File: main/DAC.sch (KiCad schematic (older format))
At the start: 14 parts, among them IC3 PCM1741E, J7 Breakout I2S

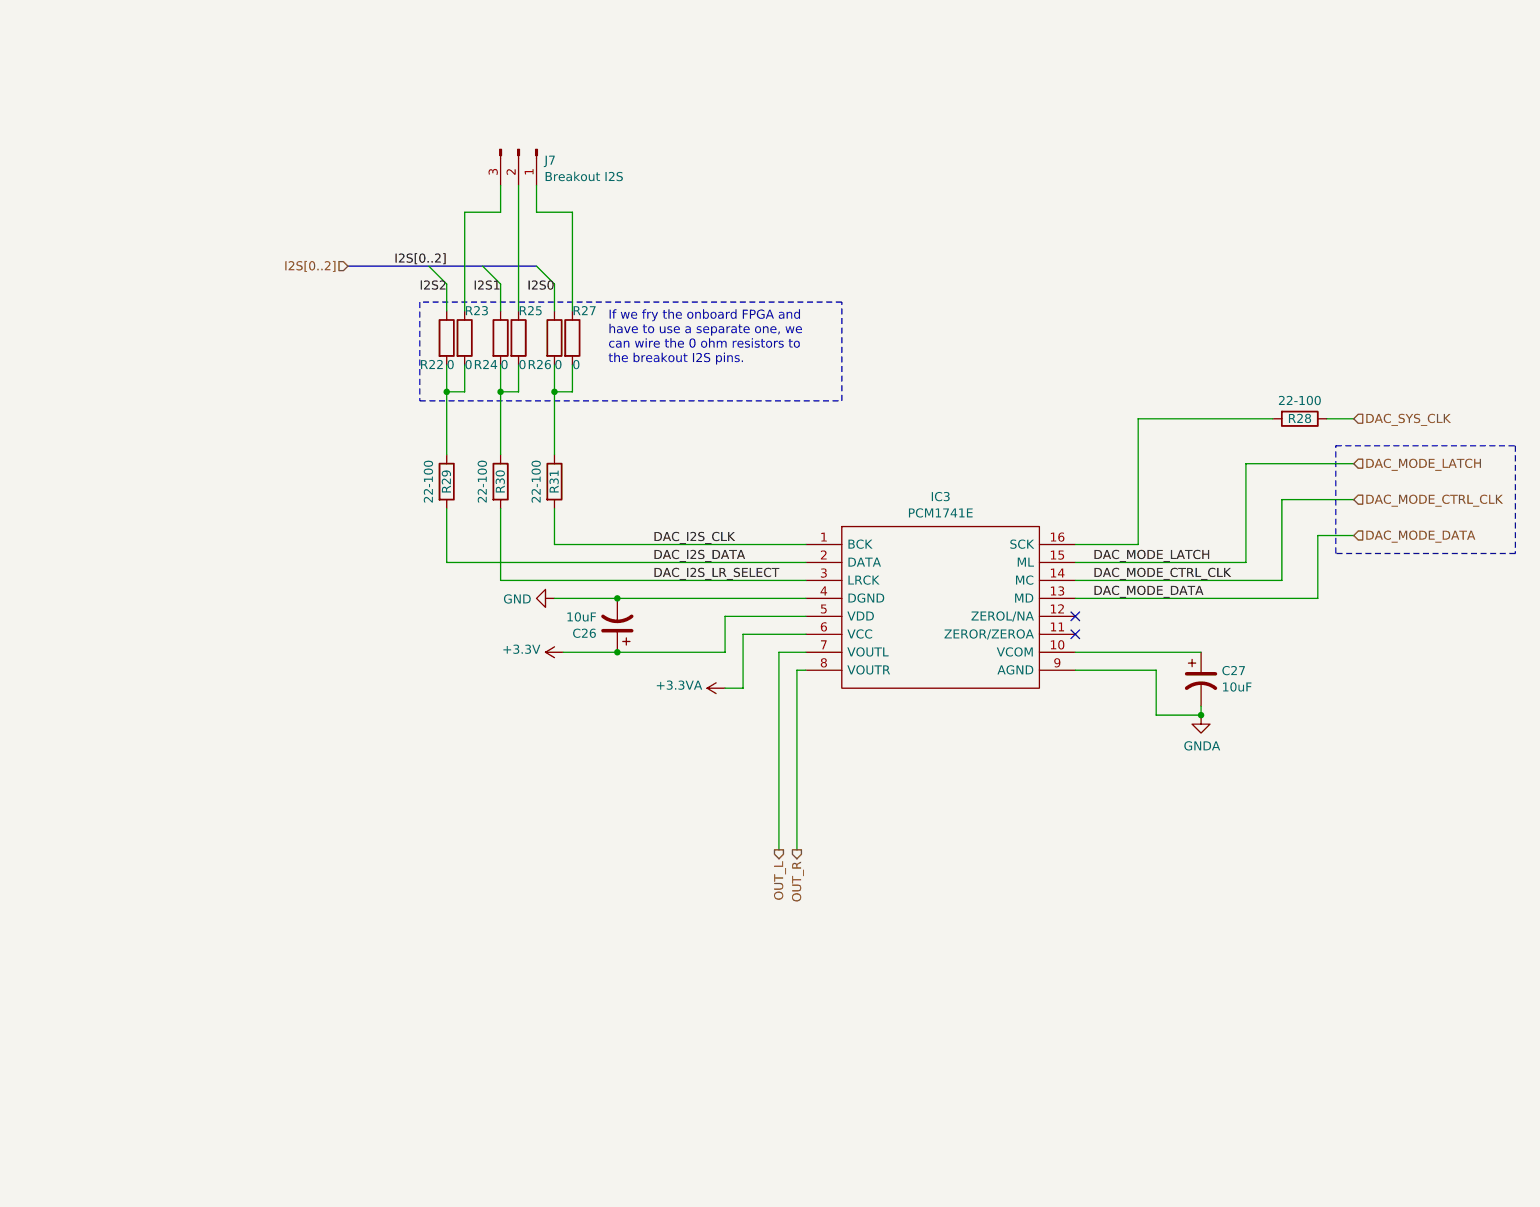
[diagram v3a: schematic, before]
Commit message: DAC: Remove amplifier, replace with low pass as per datasheet
Also: a lot of footprint association
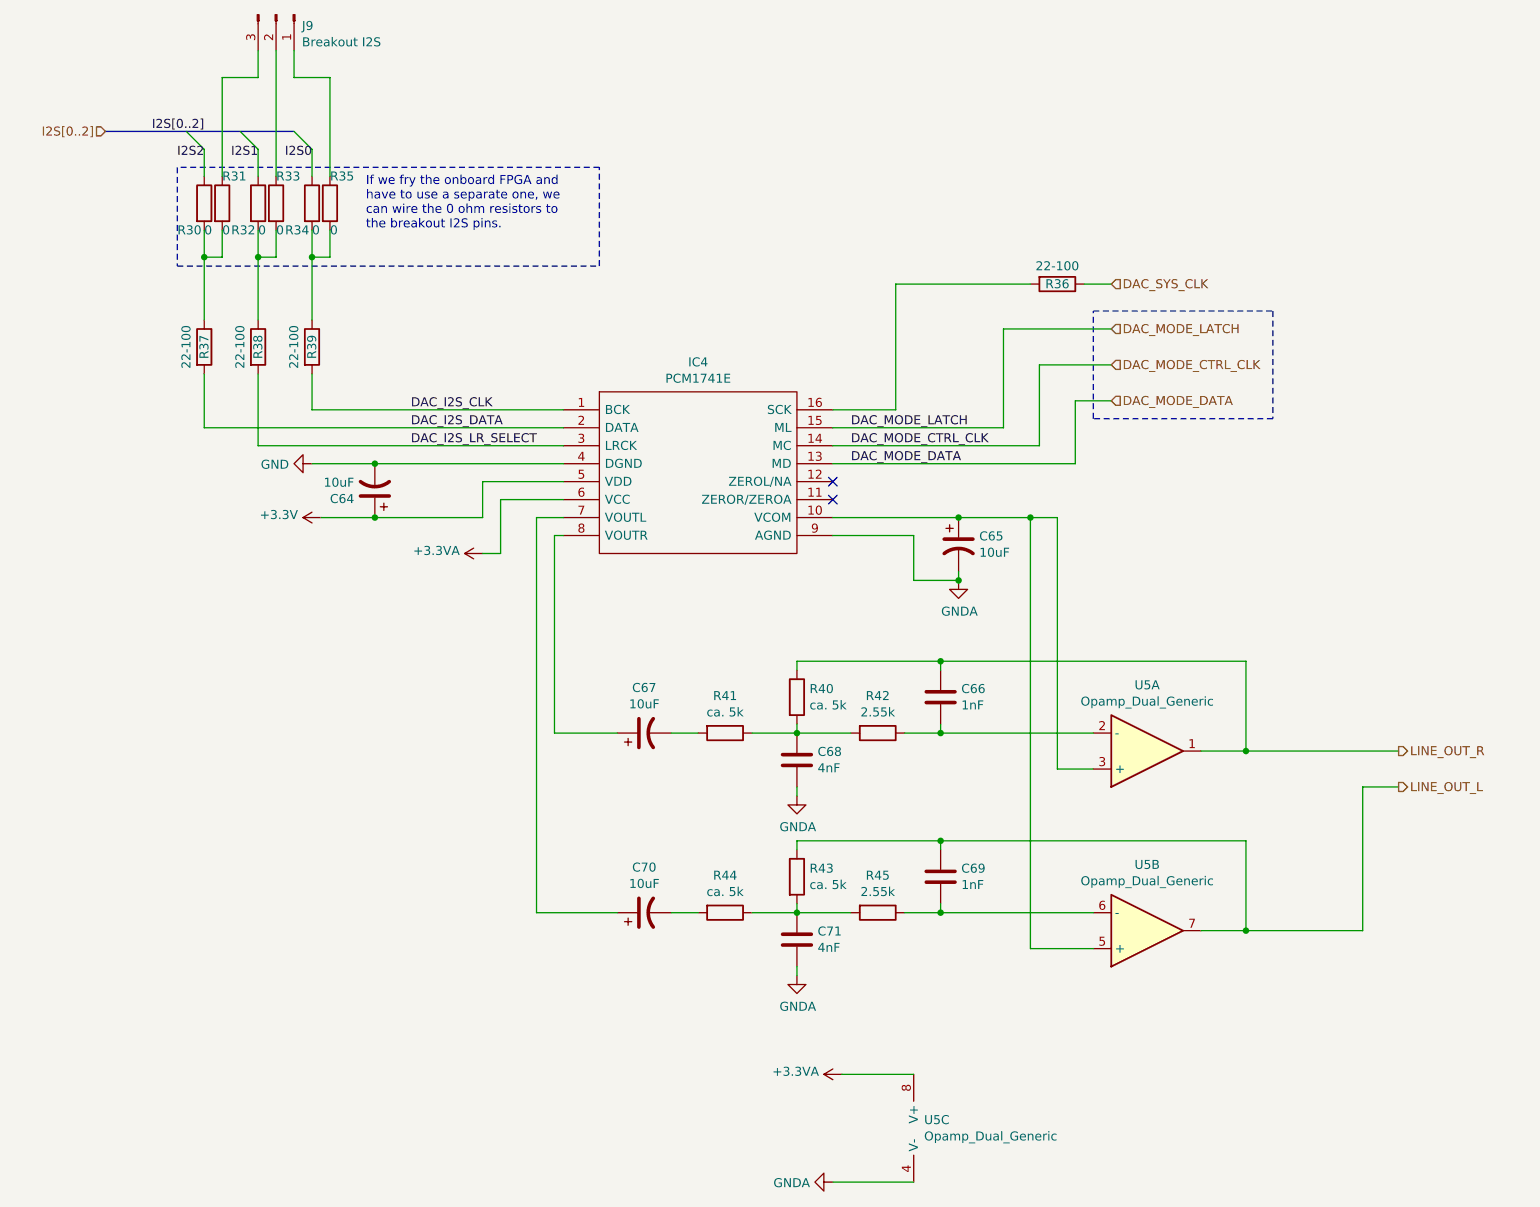
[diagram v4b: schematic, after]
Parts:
- added C66, C69: 1nF, Capacitor_SMD:C_0805_2012Metric_Pad1.18x1.45mm_HandSolder, symbol Device:C
- added C67, C70: 10uF, Capacitor_Tantalum_SMD:CP_EIA-3528-12_Kemet-T_Pad1.50x2.35mm_HandSolder, symbol Device:CP1
- added C68, C71: 4nF, Capacitor_SMD:C_0805_2012Metric_Pad1.18x1.45mm_HandSolder, symbol Device:C
- added R40, R41, R43, R44: ca. 5k, Resistor_SMD:R_0805_2012Metric_Pad1.20x1.40mm_HandSolder, symbol Device:R
- added R42, R45: 2.55k, Resistor_SMD:R_0805_2012Metric_Pad1.20x1.40mm_HandSolder, symbol Device:R
- added U5: Opamp_Dual_Generic, Package_SO:SOIC-8_5.23x5.23mm_P1.27mm, symbol Device:Opamp_Dual_Generic
- C64: renamed from C26; footprint (none) -> Capacitor_Tantalum_SMD:CP_EIA-3528-12_Kemet-T_Pad1.50x2.35mm_HandSolder
- C65: renamed from C27; footprint (none) -> Capacitor_Tantalum_SMD:CP_EIA-3528-12_Kemet-T_Pad1.50x2.35mm_HandSolder
- J9: renamed from J7; footprint (none) -> Connector_PinHeader_2.54mm:PinHeader_1x03_P2.54mm_Vertical
- renumbered IC3 to IC4, R22 to R30, R23 to R31, R24 to R32, R25 to R33, R26 to R34, R27 to R35, R28 to R36, R29 to R37, R30 to R38, R31 to R39
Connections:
- net +3.3VA: now also U5.8 (V+)
- net GNDA: now also C68.2, C71.2, U5.4 (V-)
- net at C65.1, IC4.10 (VCOM): now also U5.3 (+), U5.5 (+)
- net OUT_L: no longer names the net of IC4.7 (VOUTL)
- net OUT_L: now also C70.1
- net OUT_R: no longer names the net of IC4.8 (VOUTR)
- net OUT_R: now also C67.1
- new net: C66.2, R42.1, U5.2 (-)
- new net: C69.2, R45.1, U5.6 (-)
- new net: C68.1, R40.2, R41.1, R42.2
- new net: C67.2, R41.2
- new net: C71.1, R43.2, R44.1, R45.2
- new net: C70.2, R44.2
- new net LINE_OUT_L: C69.1, R43.1, U5.7
- new net LINE_OUT_R: C66.1, R40.1, U5.1
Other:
- moved on the sheet: C64, C65, IC4, J9, R30, R31, R32, R33, R34, R35, R36, R37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

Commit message: Start PCB layout
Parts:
- IC4: URL (none) -> https://www.digikey.no/product-detail/no/texas-instruments/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
- J9: Comment (none) -> Same as FPGA_GPIO (Cut to length)
- U5: Description (none) -> OPAMP for low pass filter after DAC; Manufacturer_Name (none) -> Texas Instruments; Manufacturer_Part_Number (none) -> OPA2353UA; URL (none) -> https://www.digikey.no/product-detail/en/texas-instruments/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
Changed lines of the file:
@@
 F 2 "Connector_PinHeader_2.54mm:PinHeader_1x03_P2.54mm_Vertical" H 2100 700 50  0001 C CNN
 F 3 "~" H 2100 700 50  0001 C CNN
+F 4 "Same as FPGA_GPIO (Cut to length)" H 2100 700 50  0001 C CNN "Comment"
 	1    2100 700
 	0    1    1    0
@@
 F 10 "PCM1741E" H 5050 2200 50  0001 L CNN "Arrow Part Number"
 F 11 "https://www.arrow.com/en/products/pcm1741e/texas-instruments" H 5050 2100 50  0001 L CNN "Arrow Price/Stock"
+F 12 "https://www.digikey.no/product-detail/no/texas-instruments/PCM1741E/PCM1741E-ND/380269" H 3700 2900 50  0001 C CNN "URL"
 	1    3700 2900
 	1    0    0    -1
@@
 F 1 "Opamp_Dual_Generic" H 6950 5524 50  0000 C CNN
 F 2 "Package_SO:SOIC-8_5.23x5.23mm_P1.27mm" H 6950 5800 50  0001 C CNN
-F 3 "~" H 6950 5800 50  0001 C CNN
+F 3 "https://rocelec.widen.net/view/pdf/vkzouxzikr/sbos103.pdf?t.download=true&u=5oefqw" H 6950 5800 50  0001 C CNN
+F 4 "OPAMP for low pass filter after DAC" H 6950 5800 50  0001 C CNN "Description"
+F 5 "Texas Instruments" H 6950 5800 50  0001 C CNN "Manufacturer_Name"
+F 6 " OPA2353UA " H 6950 5800 50  0001 C CNN "Manufacturer_Part_Number"
+F 7 "https://www.digikey.no/product-detail/en/texas-instruments/OPA2353UA/OPA2353UA-ND/275849" H 6950 5800 50  0001 C CNN "URL"
 	2    6950 5800
 	1    0    0    1
@@
 F 1 "Opamp_Dual_Generic" H 5708 6855 50  0000 L CNN
 F 2 "Package_SO:SOIC-8_5.23x5.23mm_P1.27mm" H 5750 6900 50  0001 C CNN
-F 3 "~" H 5750 6900 50  0001 C CNN
+F 3 "https://rocelec.widen.net/view/pdf/vkzouxzikr/sbos103.pdf?t.download=true&u=5oefqw" H 5750 6900 50  0001 C CNN
+F 4 "OPAMP for low pass filter after DAC" H 5750 6900 50  0001 C CNN "Description"
+F 5 "Texas Instruments" H 5750 6900 50  0001 C CNN "Manufacturer_Name"
+F 6 " OPA2353UA " H 5750 6900 50  0001 C CNN "Manufacturer_Part_Number"
+F 7 "https://www.digikey.no/product-detail/en/texas-instruments/OPA2353UA/OPA2353UA-ND/275849" H 5750 6900 50  0001 C CNN "URL"
 	3    5750 6900
 	1    0    0    -1
@@
 F 1 "Opamp_Dual_Generic" H 6950 4524 50  0000 C CNN
 F 2 "Package_SO:SOIC-8_5.23x5.23mm_P1.27mm" H 6950 4800 50  0001 C CNN
-F 3 "~" H 6950 4800 50  0001 C CNN
+F 3 "https://rocelec.widen.net/view/pdf/vkzouxzikr/sbos103.pdf?t.download=true&u=5oefqw" H 6950 4800 50  0001 C CNN
+F 4 "OPAMP for low pass filter after DAC" H 6950 4800 50  0001 C CNN "Description"
+F 5 "Texas Instruments" H 6950 4800 50  0001 C CNN "Manufacturer_Name"
+F 6 " OPA2353UA " H 6950 4800 50  0001 C CNN "Manufacturer_Part_Number"
+F 7 "https://www.digikey.no/product-detail/en/texas-instruments/OPA2353UA/OPA2353UA-ND/275849" H 6950 4800 50  0001 C CNN "URL"
 	1    6950 4800
 	1    0    0    1
